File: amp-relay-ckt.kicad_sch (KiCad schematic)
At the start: 13 parts, among them K11 HK19F-DCxxV-SHC, Q2 Q_PNP_BCE, Q5 BSS123, U1 LM7805_TO220

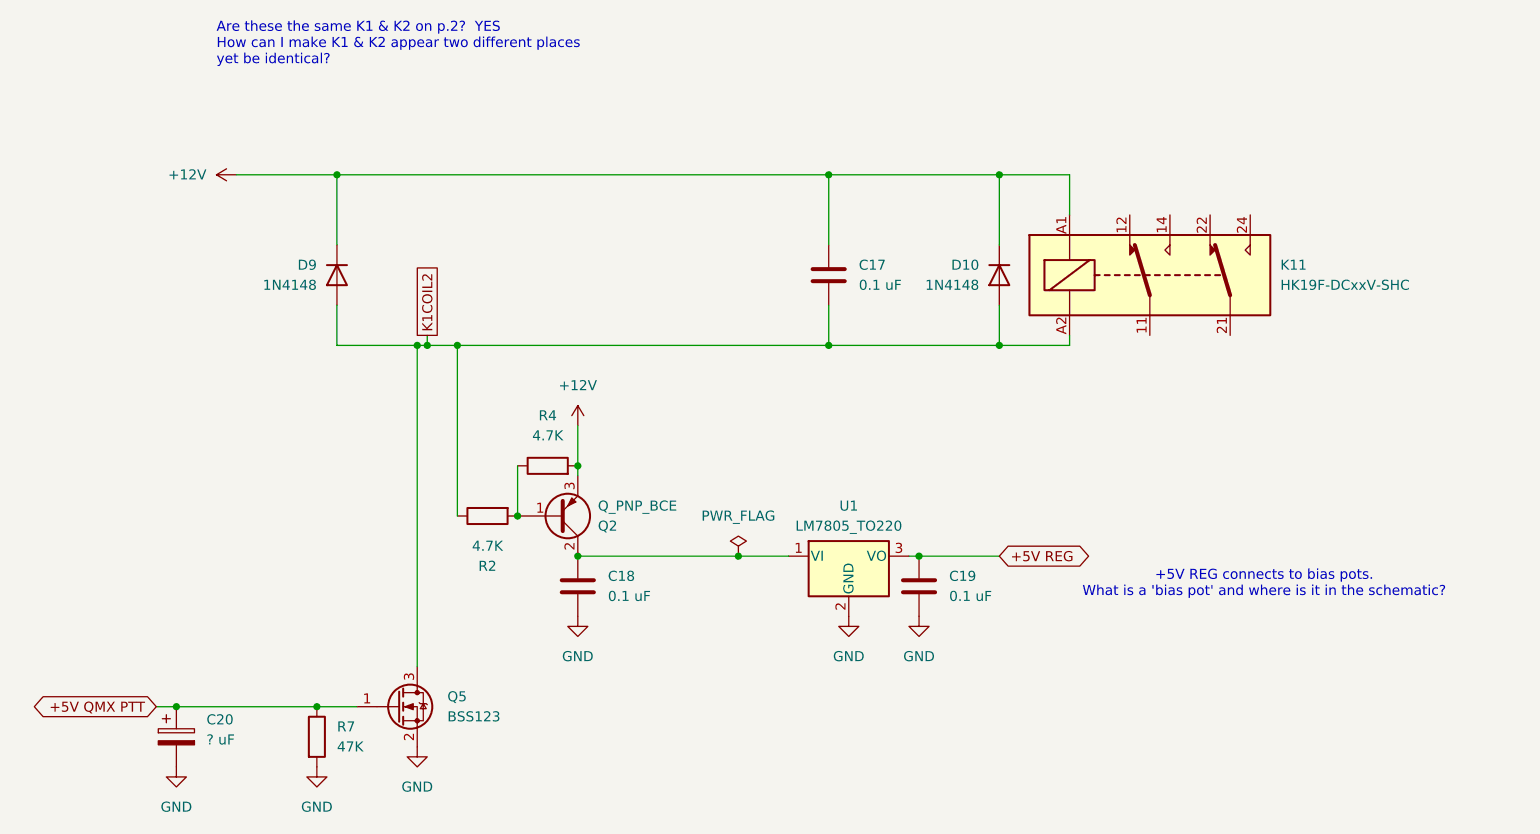
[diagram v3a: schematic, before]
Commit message: got rid of K11 which was alias for K2.  Figured out RELAY-SYNC as a way of making sure K1 & K2 operate in sync
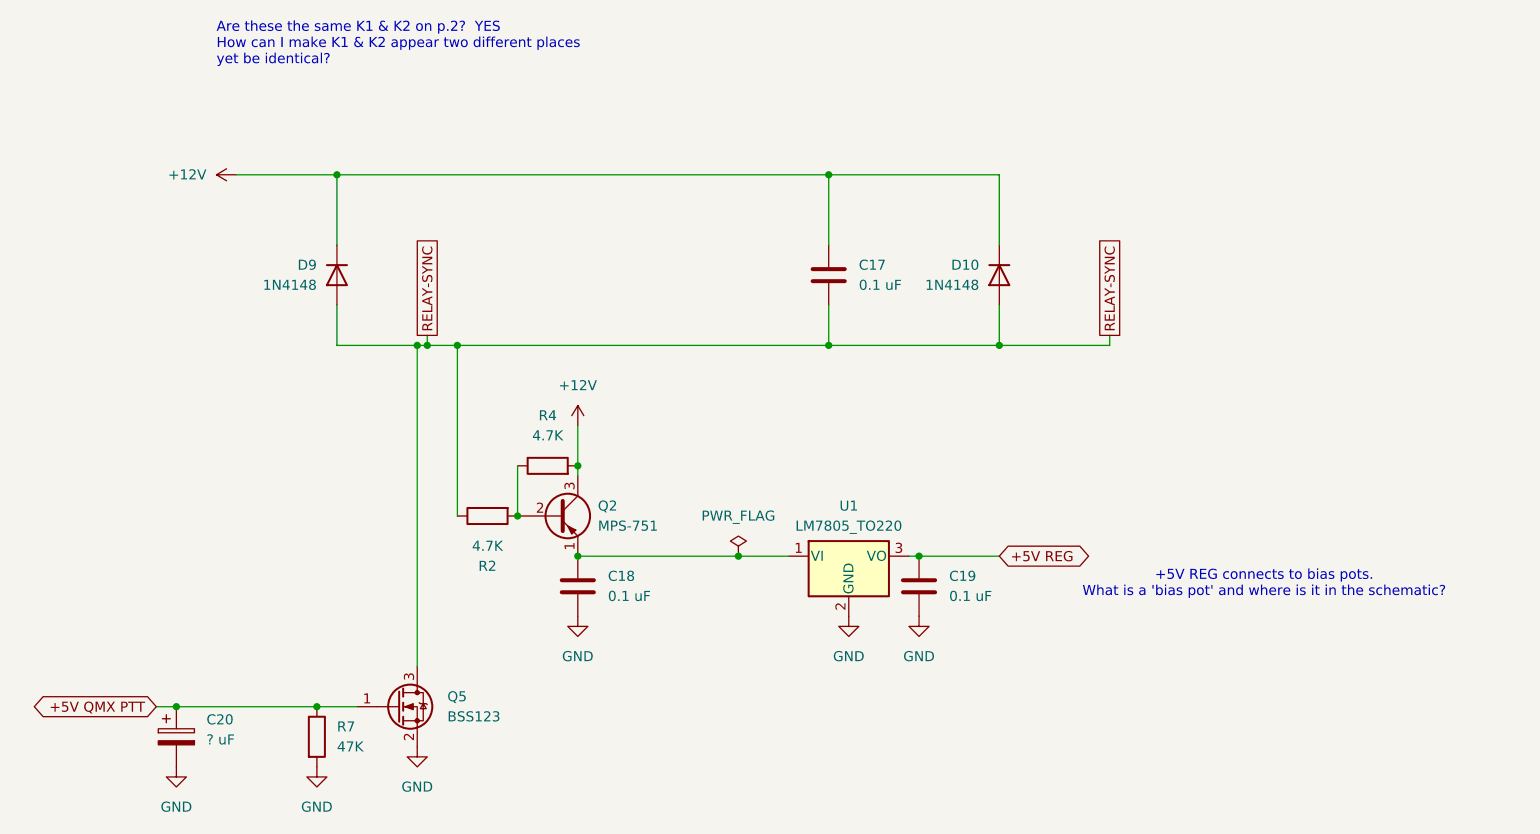
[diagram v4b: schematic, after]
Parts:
- removed K11: HK19F-DCxxV-SHC, Relay_THT:Relay_DPDT_Finder_30.22, symbol Relay:HK19F-DCxxV-SHC
- removed Q2: Q_PNP_BCE, symbol Device:Q_PNP_BCE
- added Q2: MPS-751, symbol ZZZMyLibrary:MPS-751
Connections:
- net +12V: now also Q2.3 (C)
- net at R2.2, R4.1: now also Q2.2 (B)
- net at C18.1, U1.1 (VI): now also Q2.1 (E)
- net K1COIL2 renamed RELAY-SYNC
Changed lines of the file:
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@@
+	)
+	(junction
+		(at 156.21 74.93)
+		(diameter 0)
+		(color 0 0 0 0)
+	)
+	(junction
+		(at 87.63 74.93)
+		(diameter 0)
+		(color 0 0 0 0)
+	)
+	(junction
+		(at 102.87 101.6)
+		(diameter 0)
+		(color 0 0 0 0)
+	)
+	(junction
+		(at 72.39 53.34)
+		(diameter 0)
+		(color 0 0 0 0)
+	)
+	(junction
+		(at 82.55 74.93)
+		(diameter 0)
+		(color 0 0 0 0)
+	)
+	(junction
+		(at 52.07 120.65)
+		(diameter 0)
+		(color 0 0 0 0)
+	)
+	(junction
+		(at 83.82 74.93)
+		(diameter 0)
+		(color 0 0 0 0)
+	)
+	(junction
+		(at 134.62 53.34)
+		(diameter 0)
+		(color 0 0 0 0)
+	)
+	(junction
+		(at 102.87 90.17)
+		(diameter 0)
+		(color 0 0 0 0)
 	)
 	(junction
@@
 	)
 	(junction
-		(at 156.21 53.34)
-		(diameter 0)
-		(color 0 0 0 0)
-	)
-	(junction
-		(at 102.87 101.6)
-		(diameter 0)
-		(color 0 0 0 0)
-	)
-	(junction
-		(at 87.63 74.93)
-		(diameter 0)
-		(color 0 0 0 0)
-	)
-	(junction
-		(at 156.21 74.93)
-		(diameter 0)
-		(color 0 0 0 0)
-	)
-	(junction
-		(at 72.39 53.34)
-		(diameter 0)
-		(color 0 0 0 0)
-	)
-	(junction
-		(at 82.55 74.93)
-		(diameter 0)
-		(color 0 0 0 0)
-	)
-	(junction
-		(at 52.07 120.65)
-		(diameter 0)
-		(color 0 0 0 0)
-	)
-	(junction
-		(at 83.82 74.93)
-		(diameter 0)
-		(color 0 0 0 0)
-	)
-	(junction
-		(at 134.62 53.34)
-		(diameter 0)
-		(color 0 0 0 0)
-	)
-	(junction
-		(at 102.87 90.17)
-		(diameter 0)
-		(color 0 0 0 0)
-	)
-	(junction
 		(at 123.19 101.6)
 		(diameter 0)
@@
 	(wire
 		(pts
+			(xy 170.18 74.93) (xy 170.18 73.66)
+		)
+		(stroke
+			(width 0)
+			(type default)
+		)
+	)
+	(wire
+		(pts
 			(xy 72.39 74.93) (xy 82.55 74.93)
 		)
@@
 	(wire
 		(pts
-			(xy 165.1 73.66) (xy 165.1 74.93)
-		)
-		(stroke
-			(width 0)
-			(type default)
-		)
-	)
-	(wire
-		(pts
-			(xy 165.1 74.93) (xy 156.21 74.93)
+			(xy 156.21 74.93) (xy 170.18 74.93)
 		)
 		(stroke
@@
 	(wire
 		(pts
-			(xy 165.1 53.34) (xy 165.1 58.42)
-		)
-		(stroke
-			(width 0)
-			(type default)
-		)
-	)
-	(wire
-		(pts
 			(xy 83.82 74.93) (xy 87.63 74.93)
 		)
@@
 		(pts
 			(xy 83.82 73.66) (xy 83.82 74.93)
-		)
-		(stroke
-			(width 0)
-			(type default)
-		)
-	)
-	(wire
-		(pts
-			(xy 156.21 53.34) (xy 165.1 53.34)
 		)
 		(stroke
@@
 		)
 	)
+	(global_label "RELAY-SYNC"
+		(shape passive)
+		(at 170.18 73.66 90)
+		(fields_autoplaced yes)
+		(effects
+			(font
+				(size 1.27 1.27)
+			)
+			(justify left)
+		)
+		(property "Intersheetrefs" "${INTERSHEET_REFS}"
+			(at 170.18 59.5004 90)
+			(effects
+				(font
+					(size 1.27 1.27)
+				)
+				(justify left)
+				(hide yes)
+			)
+		)
+	)
 	(global_label "+5V REG"
 		(shape bidirectional)
@@
 		)
 	)
-	(global_label "K1COIL2"
+	(global_label "RELAY-SYNC"
 		(shape passive)
 		(at 83.82 73.66 90)
@@
 		)
 		(property "Intersheetrefs" "${INTERSHEET_REFS}"
-			(at 83.82 63.6733 90)
+			(at 83.82 59.5004 90)
 			(effects
 				(font
@@
 	)
 	(symbol
-		(lib_id "Device:Q_PNP_BCE")
-		(at 100.33 96.52 0)
-		(mirror x)
-		(unit 1)
-		(exclude_from_sim no)
-		(in_bom yes)
-		(on_board yes)
-		(dnp no)
-		(property "Reference" "Q2"
-			(at 105.41 97.7901 0)
-			(effects
-				(font
-					(size 1.27 1.27)
-				)
-				(justify left)
-			)
-		)
-		(property "Value" "Q_PNP_BCE"
-			(at 105.41 95.2501 0)
-			(effects
-				(font
-					(size 1.27 1.27)
-				)
-				(justify left)
-			)
-		)
-		(property "Footprint" ""
-			(at 105.41 99.06 0)
-			(effects
-				(font
-					(size 1.27 1.27)
-				)
-				(hide yes)
-			)
-		)
-		(property "Datasheet" "~"
-			(at 100.33 96.52 0)
-			(effects
-				(font
-					(size 1.27 1.27)
-				)
-				(hide yes)
-			)
-		)
-		(property "Description" "PNP transistor, base/collector/emitter"
-			(at 100.33 96.52 0)
-			(effects
-				(font
-					(size 1.27 1.27)
-				)
-				(hide yes)
-			)
-		)
-		(pin "1"
-		)
-		(pin "2"
-		)
-		(pin "3"
-		)
-		(instances
-			(project "QMX-amp"
-				(path "/e63e39d7-6ac0-4ffd-8aa3-1841a4541b55/6e8a5723-6162-4126-acdf-190058cf1f27"
-					(reference "Q2")
-					(unit 1)
-				)
-			)
-		)
-	)
-	(symbol
 		(lib_id "power:GND")
 		(at 102.87 109.22 0)
@@
 	)
 	(symbol
-		(lib_id "Relay:HK19F-DCxxV-SHC")
-		(at 175.26 66.04 0)
-		(unit 1)
-		(exclude_from_sim no)
-		(in_bom yes)
-		(on_board yes)
-		(dnp no)
-		(fields_autoplaced yes)
-		(property "Reference" "K11"
-			(at 191.77 64.7699 0)
-			(effects
-				(font
-					(size 1.27 1.27)
-				)
-				(justify left)
-			)
-		)
-		(property "Value" "HK19F-DCxxV-SHC"
-			(at 191.77 67.3099 0)
-			(effects
-				(font
-					(size 1.27 1.27)
-				)
-				(justify left)
-			)
-		)
-		(property "Footprint" "Relay_THT:Relay_DPDT_Finder_30.22"
-			(at 157.48 78.74 0)
-			(effects
-				(font
-					(size 1.27 1.27)
-				)
-				(justify left)
-				(hide yes)
-			)
-		)
-		(property "Datasheet" "https://www.lcsc.com/datasheet/lcsc_datasheet_1810201512_Ningbo-Keke-New-Era-Appliance-HK19F-DC12V-SHG_C42803.pdf"
-			(at 175.26 83.82 0)
-			(effects
-				(font
-					(size 1.27 1.27)
-				)
-				(hide yes)
-			)
-		)
-		(property "Description" "HuiKe 19F monostable relay, DPDT, 1A"
-			(at 176.53 81.28 0)
-			(effects
-				(font
-					(size 1.27 1.27)
-				)
-				(hide yes)
-			)
-		)
-		(pin "A2"
-		)
-		(pin "A1"
-		)
-		(pin "22"
-		)
-		(pin "21"
-		)
-		(pin "24"
-		)
-		(pin "14"
-		)
-		(pin "12"
-		)
-		(pin "11"
-		)
-		(instances
-			(project "QMX-amp"
-				(path "/e63e39d7-6ac0-4ffd-8aa3-1841a4541b55/6e8a5723-6162-4126-acdf-190058cf1f27"
-					(reference "K11")
-					(unit 1)
-				)
-			)
-		)
-	)
-	(symbol
 		(lib_id "power:GND")
 		(at 146.05 109.22 0)
@@
 					(unit 1)
 				)
+			)
+		)
+	)
+	(symbol
+		(lib_id "ZZZMyLibrary:MPS-751")
+		(at 100.33 96.52 0)
+		(unit 1)
+		(exclude_from_sim no)
+		(in_bom yes)
+		(on_board yes)
+		(dnp no)
+		(fields_autoplaced yes)
+		(property "Reference" "Q2"
+			(at 105.41 95.2499 0)
+			(effects
+				(font
+					(size 1.27 1.27)
+				)
+				(justify left)
+			)
+		)
+		(property "Value" "MPS-751"
+			(at 105.41 97.7899 0)
+			(effects
+				(font
+					(size 1.27 1.27)
+				)
+				(justify left)
+			)
+		)
+		(property "Footprint" ""
+			(at 105.41 93.98 0)
+			(effects
+				(font
+					(size 1.27 1.27)
+				)
+				(hide yes)
+			)
+		)
+		(property "Datasheet" "~"
+			(at 100.33 96.52 0)
+			(effects
+				(font
+					(size 1.27 1.27)
+				)
+				(hide yes)
+			)
+		)
+		(property "Description" "PNP transistor, emitter/base/collector"
+			(at 100.33 96.52 0)
+			(effects
+				(font
+					(size 1.27 1.27)
+				)
+				(hide yes)
+			)
+		)
+		(pin "1"
+		)
+		(pin "3"
+		)
+		(pin "2"
+		)
+		(instances
+			(project ""
+				(path "/e63e39d7-6ac0-4ffd-8aa3-1841a4541b55/6e8a5723-6162-4126-acdf-190058cf1f27"
+					(reference "Q2")
+					(unit 1)
+				)
